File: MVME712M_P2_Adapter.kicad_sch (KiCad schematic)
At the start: 12 parts, among them J1 Conn_01x05_Pin, J2 DIN41612_03x32_C_Split, J3 Conn_02x25_Odd_Even, P2 DIN41612_03x32_C_Split

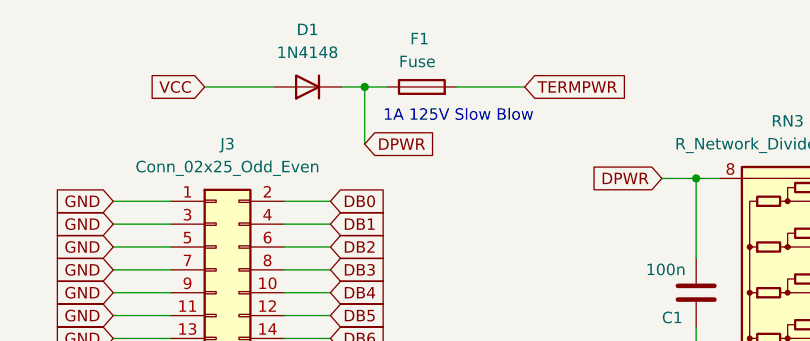
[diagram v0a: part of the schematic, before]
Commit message: added RS232 text
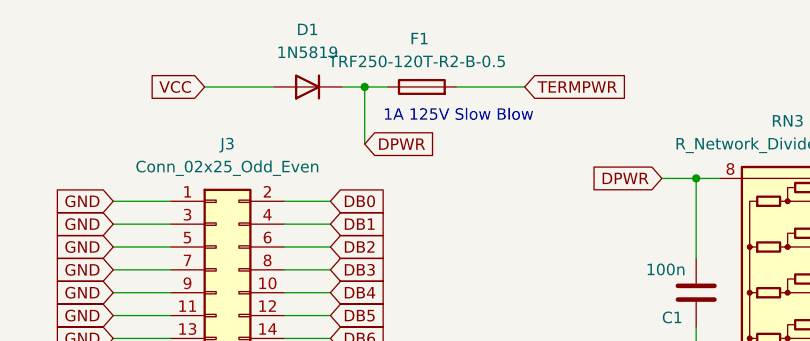
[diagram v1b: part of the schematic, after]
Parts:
- D1: value 1N4148 -> 1N5819
- F1: value Fuse -> TRF250-120T-R2-B-0.5; footprint Fuse:Fuse_2512_6332Metric_Pad1.52x3.35mm_HandSolder -> Fuse:Fuse_Bourns_MF-RG500
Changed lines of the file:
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@@
 			)
 		)
-		(property "Value" "Fuse"
+		(property "Value" "TRF250-120T-R2-B-0.5"
 			(at 216.662 17.526 90)
 			(effects
@@
 			)
 		)
-		(property "Footprint" "Fuse:Fuse_2512_6332Metric_Pad1.52x3.35mm_HandSolder"
+		(property "Footprint" "Fuse:Fuse_Bourns_MF-RG500"
 			(at 217.17 22.098 90)
 			(effects
@@
 			)
 		)
-		(property "Value" "1N4148"
+		(property "Value" "1N5819"
 			(at 204.47 16.51 0)
 			(effects
